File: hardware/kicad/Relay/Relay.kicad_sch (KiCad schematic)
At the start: 14 parts, among them J1 Conn_02x04_Odd_Even, J2 Conn_02x04_Odd_Even, K1 FINDER-34.51, K2 FINDER-34.51, Q1 BC817, Q2 BC817

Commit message: Initial Create of Empty Module-Board
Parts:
- J1, J2: footprint Connector_PinSocket_2.54mm:PinSocket_2x04_P2.54mm_Vertical -> EnvNode:PinSocket_2x04_P2.54mm_Vertical_Bottom
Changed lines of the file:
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@@
 			)
 		)
-		(property "Footprint" "Connector_PinSocket_2.54mm:PinSocket_2x04_P2.54mm_Vertical"
+		(property "Footprint" "EnvNode:PinSocket_2x04_P2.54mm_Vertical_Bottom"
 			(at 92.71 46.99 0)
 			(hide yes)
@@
 			)
 		)
-		(property "Footprint" "Connector_PinSocket_2.54mm:PinSocket_2x04_P2.54mm_Vertical"
+		(property "Footprint" "EnvNode:PinSocket_2x04_P2.54mm_Vertical_Bottom"
 			(at 52.07 46.99 0)
 			(hide yes)

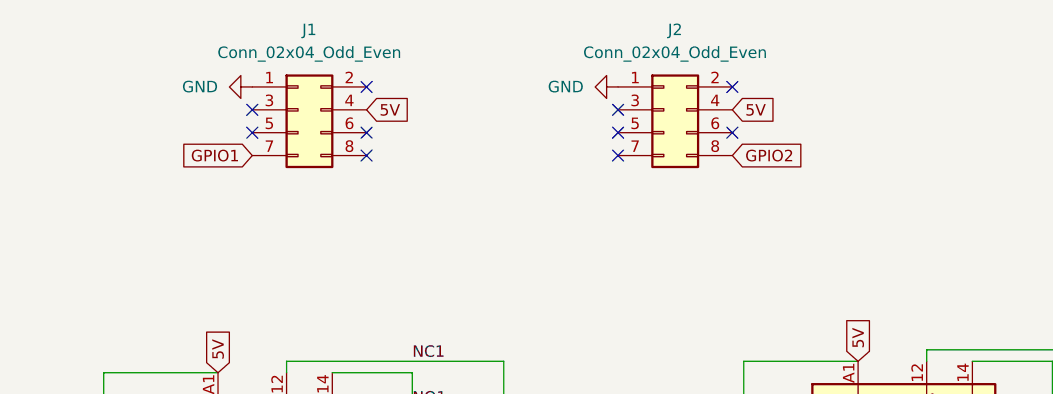
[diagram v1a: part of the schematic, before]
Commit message: Updated Relay-Board with DesignBlock
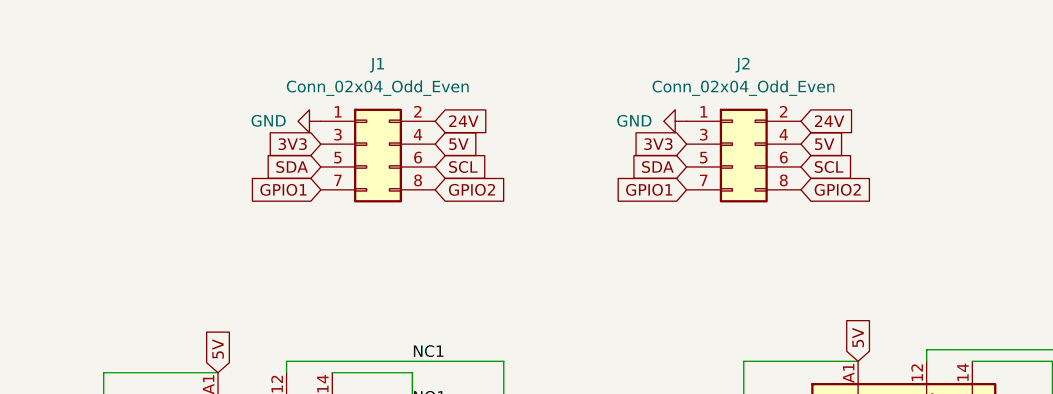
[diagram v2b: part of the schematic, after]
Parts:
- J1, J2: footprint EnvNode:PinSocket_2x04_P2.54mm_Vertical_Bottom -> Connector_PinSocket_2.54mm:PinSocket_2x04_P2.54mm_Vertical
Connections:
- net GPIO1: now also J2.7 (Pin_7)
- net GPIO2: now also J1.8 (Pin_8)
- net 24V: now reaches J2.2 (Pin_2)
- net 24V: now also J1.2 (Pin_2)
- net 3V3: now reaches J2.3 (Pin_3)
- net 3V3: now also J1.3 (Pin_3)
- net SDA: now reaches J2.5 (Pin_5)
- net SDA: now also J1.5 (Pin_5)
- net SCL: now reaches J2.6 (Pin_6)
- net SCL: now also J1.6 (Pin_6)
- no-connect marks 10 -> 0
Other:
- moved on the sheet: J1
